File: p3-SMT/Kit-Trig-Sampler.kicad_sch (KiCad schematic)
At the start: 81 parts, among them J1 START_CV, J10 AUDIO_INR, J11 AUDIO_OUTL, J13 BANK_CV, J14 Eurorack_Power_10pin_Unshroud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, J2 LENGTH_CV, J3 SAMP_CV, J4 PITCH CV, J5 REV_TRIG, J6 PLAY_TRIG, J7 END_OUT, J8 AUDIO_INL, J9 AUIDO_OUTR, U1 NJM2068, U2 NJM2068, U3 AZ1117CR-3.3TRG1

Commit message: p3 SMT: added 47K resistors to Trig Ins
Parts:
- added R17, R20: 47k_0603, 4ms_Resistor:R_0603, symbol 4ms_Resistor_0603:47k_0603
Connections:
- net D13: now also R20.2; no longer J6.1 (SIG)
- net D2: now also R17.2; no longer J5.1 (SIG)
- new net: J5.1 (SIG), R17.1
- new net: J6.1 (SIG), R20.1
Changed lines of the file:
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@@
     (stroke (width 0) (type default))
   )
-  (wire (pts (xy 194.31 80.01) (xy 200.66 80.01))
+  (wire (pts (xy 194.31 80.01) (xy 199.39 80.01))
     (stroke (width 0) (type default))
   )
@@
     (stroke (width 0) (type default))
   )
+  (wire (pts (xy 207.01 49.53) (xy 215.9 49.53))
+    (stroke (width 0) (type default))
+  )
   (wire (pts (xy 210.82 129.54) (xy 215.9 129.54))
     (stroke (width 0) (type default))
@@
     (stroke (width 0) (type default))
   )
-  (wire (pts (xy 194.31 49.53) (xy 200.66 49.53))
+  (wire (pts (xy 194.31 49.53) (xy 199.39 49.53))
     (stroke (width 0) (type default))
   )
@@
     (stroke (width 0) (type default))
   )
+  (wire (pts (xy 207.01 80.01) (xy 215.9 80.01))
+    (stroke (width 0) (type default))
+  )
   (wire (pts (xy 466.09 247.65) (xy 472.44 247.65))
     (stroke (width 0) (type default))
@@
     (stroke (width 0) (type default))
   )
-  (text "Rev_Trig" (at 201.93 48.895 0)
+  (text "Rev_Trig" (at 217.17 48.895 0)
     (effects (font (size 1.27 1.27)) (justify left bottom))
   )
@@
     (effects (font (size 1.27 1.27)) (justify left bottom))
   )
-  (text "Play_Trig" (at 201.93 80.01 0)
+  (text "Play_Trig" (at 217.17 80.01 0)
     (effects (font (size 1.27 1.27)) (justify left bottom))
   )
@@
     (effects (font (size 1.27 1.27)) (justify right bottom))
   )
-  (label "D2" (at 200.66 49.53 180) (fields_autoplaced)
+  (label "D2" (at 215.9 49.53 180) (fields_autoplaced)
     (effects (font (size 1.27 1.27)) (justify right bottom))
   )
@@
     (effects (font (size 1.27 1.27)) (justify left bottom))
   )
-  (label "D13" (at 200.66 80.01 180) (fields_autoplaced)
+  (label "D13" (at 215.9 80.01 180) (fields_autoplaced)
     (effects (font (size 1.27 1.27)) (justify right bottom))
   )
@@
         (path "/39a72d2b-4494-42c9-aa7a-6ac21ca5673f"
           (reference "#PWR011") (unit 1)
+        )
+      )
+    )
+  )
+  (symbol (lib_id "4ms_Resistor_0603:47k_0603") (at 203.2 49.53 90) (unit 1)
+    (in_bom yes) (on_board yes) (dnp no) (fields_autoplaced)
+    (property "Reference" "R17" (at 203.2 44.45 90)
+      (effects (font (size 1.27 1.27)))
+    )
+    (property "Value" "47k_0603" (at 203.2 52.07 90)
+      (effects (font (size 1.27 1.27)) hide)
+    )
+    (property "Footprint" "4ms_Resistor:R_0603" (at 215.9 52.07 0)
+      (effects (font (size 1.27 1.27)) (justify left) hide)
+    )
+    (property "Datasheet" "" (at 203.2 49.53 0)
+      (effects (font (size 1.27 1.27)) hide)
+    )
+    (property "Specifications" "47k, 1%, 1/10W, 0603" (at 211.074 52.07 0)
+      (effects (font (size 1.27 1.27)) (justify left) hide)
+    )
+    (property "Manufacturer" "Yageo" (at 212.598 52.07 0)
+      (effects (font (size 1.27 1.27)) (justify left) hide)
+    )
+    (property "Part Number" "RC0603FR-0747KL" (at 214.122 52.07 0)
+      (effects (font (size 1.27 1.27)) (justify left) hide)
+    )
+    (property "Display" "47k" (at 203.2 46.99 90)
+      (effects (font (size 1.27 1.27)))
+    )
+    (property "JLCPCB ID" "C105579" (at 203.2 45.72 90)
+      (effects (font (size 1.27 1.27)) hide)
+    )
+    (pin "1")
+    (pin "2")
+    (instances
+      (project "Kit-Trig-Sampler"
+        (path "/39a72d2b-4494-42c9-aa7a-6ac21ca5673f"
+          (reference "R17") (unit 1)
         )
       )
@@
         )
       )
+    )
+  )
+  (symbol (lib_id "4ms_Resistor_0603:47k_0603") (at 203.2 80.01 90) (unit 1)
+    (in_bom yes) (on_board yes) (dnp no) (fields_autoplaced)
+    (property "Reference" "R20" (at 203.2 74.93 90)
+      (effects (font (size 1.27 1.27)))
+    )
+    (property "Value" "47k_0603" (at 203.2 82.55 90)
+      (effects (font (size 1.27 1.27)) hide)
+    )
+    (property "Footprint" "4ms_Resistor:R_0603" (at 215.9 82.55 0)
+      (effects (font (size 1.27 1.27)) (justify left) hide)
+    )
+    (property "Datasheet" "" (at 203.2 80.01 0)
+      (effects (font (size 1.27 1.27)) hide)
+    )
+    (property "Specifications" "47k, 1%, 1/10W, 0603" (at 211.074 82.55 0)
+      (effects (font (size 1.27 1.27)) (justify left) hide)
+    )
+    (property "Manufacturer" "Yageo" (at 212.598 82.55 0)
+      (effects (font (size 1.27 1.27)) (justify left) hide)
+    )
+    (property "Part Number" "RC0603FR-0747KL" (at 214.122 82.55 0)
+      (effects (font (size 1.27 1.27)) (justify left) hide)
+    )
+    (property "Display" "47k" (at 203.2 77.47 90)
+      (effects (font (size 1.27 1.27)))
+    )
+    (property "JLCPCB ID" "C105579" (at 203.2 76.2 90)
+      (effects (font (size 1.27 1.27)) hide)
+    )
+    (pin "1")
+    (pin "2")
+    (instances
+      (project "Kit-Trig-Sampler"
+        (path "/39a72d2b-4494-42c9-aa7a-6ac21ca5673f"
+          (reference "R20") (unit 1)
+        )
+      )

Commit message: p3-SMT: Updated all syms from lib
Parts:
- C1, C10, C11, C12, C13, C14, C15, C16, C17, C19, C2, C20, C3, C4, C5, C6, C7, C8, C9, D1, D2, R1, R10, R11, R12, R13, R14, R15, R16, R17, R18, R19, R2, R20, R21, R23, R25, R26, R27, R28, R3, R30, R31, R32, R33, R34, R37, R4, R40, R41, R5, R6, R7, R8, R9, U1, U2, U3: Production Stage (none) -> A
- J1: value START_CV -> 3.5mm_Mono_Switched; Production Stage (none) -> C
- J10: value AUDIO_INR -> 3.5mm_Mono_Switched; Production Stage (none) -> C
- J11: value AUDIO_OUTL -> 3.5mm_Mono_Switched; Production Stage (none) -> C
- J13: value BANK_CV -> 3.5mm_Mono_Switched; Production Stage (none) -> C
- J14: Production Stage (none) -> B
- J2: value LENGTH_CV -> 3.5mm_Mono_Switched; Production Stage (none) -> C
- J3: value SAMP_CV -> 3.5mm_Mono_Switched; Production Stage (none) -> C
- J4: value PITCH CV -> 3.5mm_Mono_Switched; Production Stage (none) -> C
- J5: value REV_TRIG -> 3.5mm_Mono_Switched; Production Stage (none) -> C
- J6: value PLAY_TRIG -> 3.5mm_Mono_Switched; Production Stage (none) -> C
- J7: value END_OUT -> 3.5mm_Mono_Switched; Production Stage (none) -> C
- J8: value AUDIO_INL -> 3.5mm_Mono_Switched; Production Stage (none) -> C
- J9: value AUIDO_OUTR -> 3.5mm_Mono_Switched; Production Stage (none) -> C
- POT_LENGTH1, POT_PITCH1, POT_SAMP1, POT_START1: Production Stage (none) -> C
- SD1: Production Stage (none) -> AB

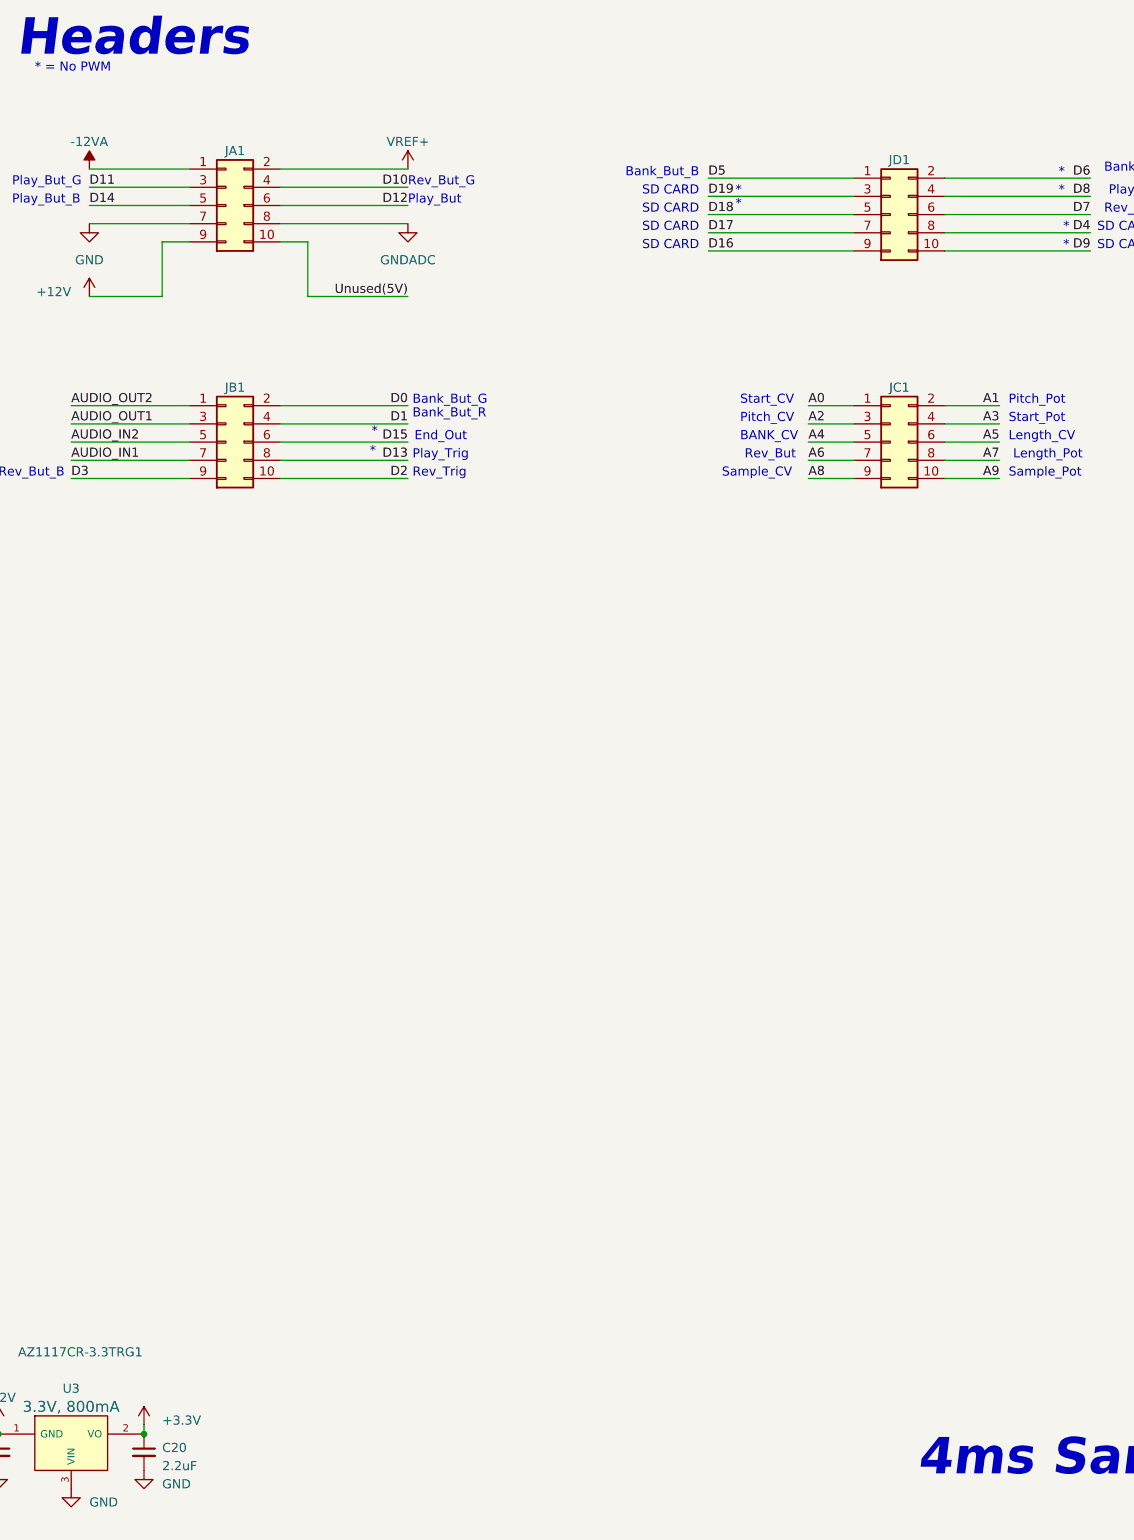
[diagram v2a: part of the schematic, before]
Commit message: p3-SMT: update socket symbols, add PCB/faceplate/knob symbols
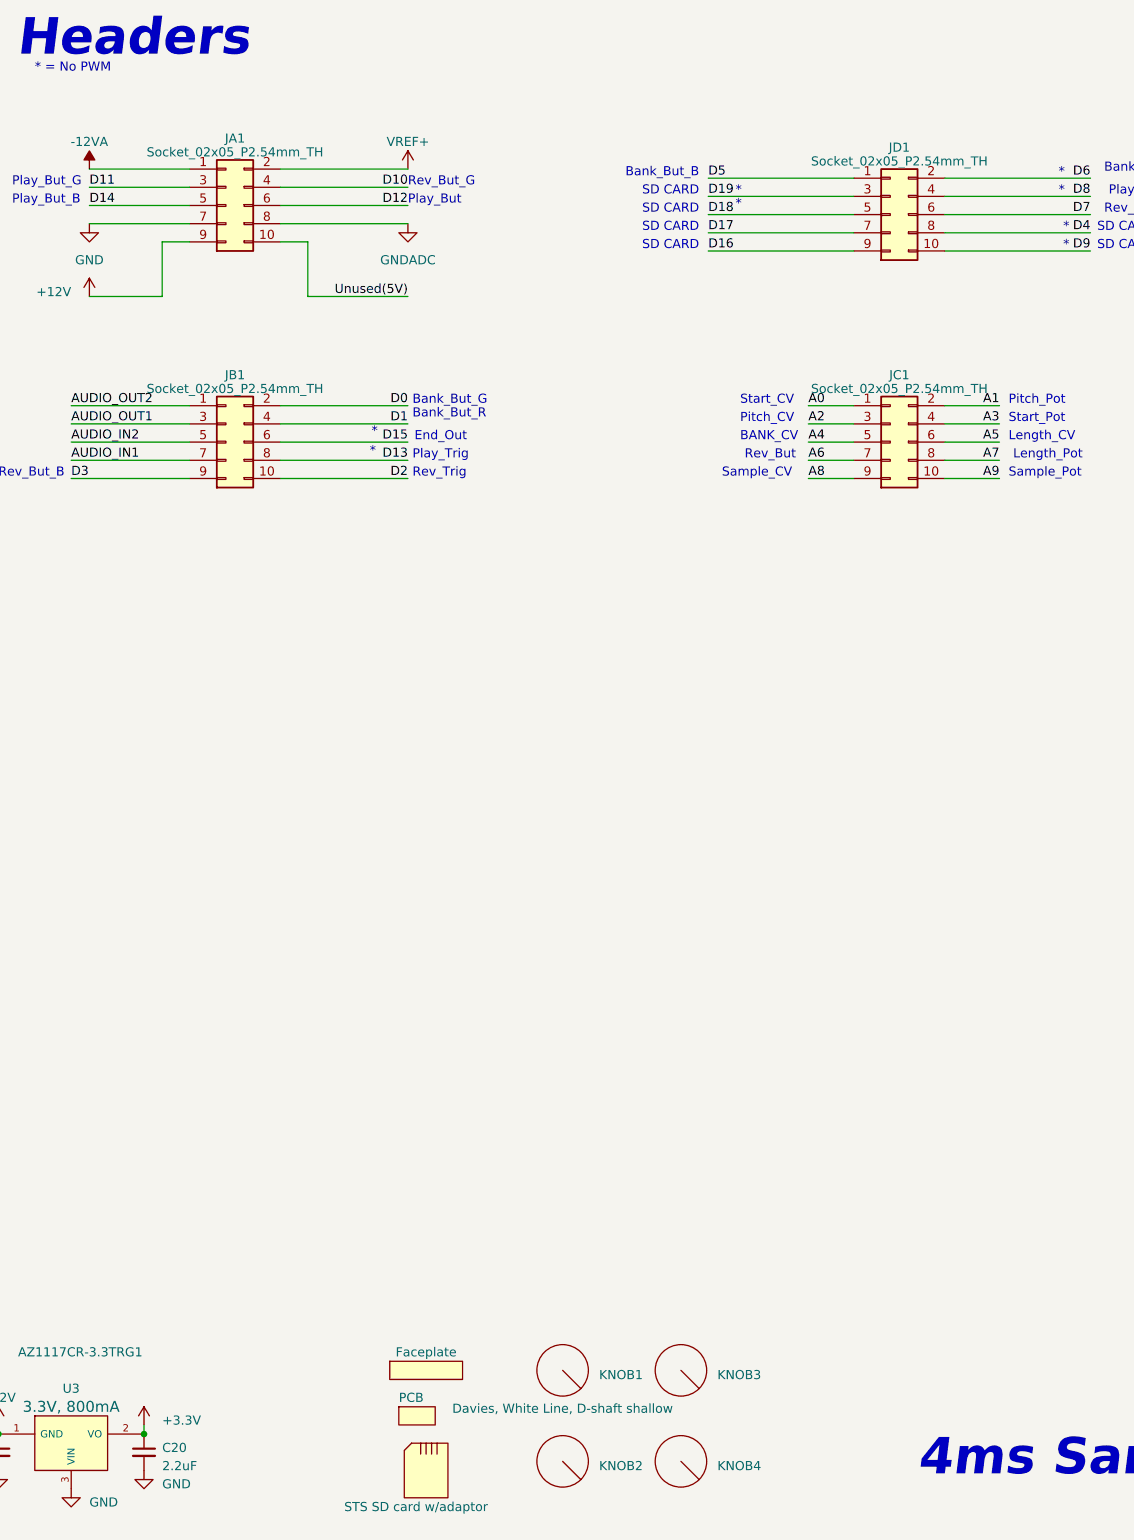
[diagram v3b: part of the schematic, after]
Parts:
- added FP1: Faceplate, symbol 4ms_Hardware:Faceplate
- added KNOB1, KNOB2, KNOB3, KNOB4: Davies, White Line, D-shaft shallow, symbol 4ms_Hardware:Knob_Davies_WhiteLine
- added PCB1: PCB, symbol 4ms_Hardware:PCB
- added U4: STS SD card w/adaptor, symbol 4ms_Hardware:microSDcard_STS
- Bank_But1, PLAY_BUT1, REV_BUT1: Production Stage (none) -> C
- JA1, JB1, JC1, JD1: value Socket_02x05_TH -> Socket_02x05_P2.54mm_TH; symbol 4ms_Connector:Socket_02x05_TH -> 4ms_Connector:Socket_02x05_P2.54mm_TH; Manufacturer (none) -> Samtec; Part Number (none) -> SSW-105-01-G-D; Production Stage (none) -> B; Specifications HEADER 2x5 FEMALE PINS 0.100” 180deg -> HEADER 2x5 FEMALE SOCKET 0.100” 180deg

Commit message: finish p3-SMT BOM. Update all headers to non-gold
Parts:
- JA1, JB1, JC1, JD1: Part Number SSW-105-01-G-D -> SSW-105-01-T-D; Specifications HEADER 2x5 FEMALE SOCKET 0.100” 180deg -> HEADER 2x5 FEMALE SOCKET 0.100” 180deg, Height=8.5mm
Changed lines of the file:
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@@
       (effects (font (size 1.27 1.27)) hide)
     )
-    (property "Specifications" "HEADER 2x5 FEMALE SOCKET 0.100” 180deg" (at 478.79 228.6 0)
+    (property "Specifications" "HEADER 2x5 FEMALE SOCKET 0.100” 180deg, Height=8.5mm" (at 478.79 228.6 0)
       (effects (font (size 1.27 1.27)) (justify left) hide)
     )
@@
       (effects (font (size 1.27 1.27)) (justify left) hide)
     )
-    (property "Part Number" "SSW-105-01-G-D" (at 478.79 223.52 0)
+    (property "Part Number" "SSW-105-01-T-D" (at 478.79 223.52 0)
       (effects (font (size 1.27 1.27)) (justify left) hide)
     )
@@
       (effects (font (size 1.27 1.27)) hide)
     )
-    (property "Specifications" "HEADER 2x5 FEMALE SOCKET 0.100” 180deg" (at 478.79 260.35 0)
+    (property "Specifications" "HEADER 2x5 FEMALE SOCKET 0.100” 180deg, Height=8.5mm" (at 478.79 260.35 0)
       (effects (font (size 1.27 1.27)) (justify left) hide)
     )
@@
       (effects (font (size 1.27 1.27)) (justify left) hide)
     )
-    (property "Part Number" "SSW-105-01-G-D" (at 478.79 255.27 0)
+    (property "Part Number" "SSW-105-01-T-D" (at 478.79 255.27 0)
       (effects (font (size 1.27 1.27)) (justify left) hide)
     )
@@
       (effects (font (size 1.27 1.27)) hide)
     )
-    (property "Specifications" "HEADER 2x5 FEMALE SOCKET 0.100” 180deg" (at 386.08 260.35 0)
+    (property "Specifications" "HEADER 2x5 FEMALE SOCKET 0.100” 180deg, Height=8.5mm" (at 386.08 260.35 0)
       (effects (font (size 1.27 1.27)) (justify left) hide)
     )
@@
       (effects (font (size 1.27 1.27)) (justify left) hide)
     )
-    (property "Part Number" "SSW-105-01-G-D" (at 386.08 255.27 0)
+    (property "Part Number" "SSW-105-01-T-D" (at 386.08 255.27 0)
       (effects (font (size 1.27 1.27)) (justify left) hide)
     )
@@
       (effects (font (size 1.27 1.27)) hide)
     )
-    (property "Specifications" "HEADER 2x5 FEMALE SOCKET 0.100” 180deg" (at 386.08 227.33 0)
+    (property "Specifications" "HEADER 2x5 FEMALE SOCKET 0.100” 180deg, Height=8.5mm" (at 386.08 227.33 0)
       (effects (font (size 1.27 1.27)) (justify left) hide)
     )
@@
       (effects (font (size 1.27 1.27)) (justify left) hide)
     )
-    (property "Part Number" "SSW-105-01-G-D" (at 386.08 222.25 0)
-      (effects (font (size 1.27 1.27)) (justify left) hide)
-    )
+    (property "Part Number" "SSW-105-01-T-D" (at 386.08 222.25 0)
+      (effects (font (size 1.27 1.27)) (justify left) hide)
+    )
